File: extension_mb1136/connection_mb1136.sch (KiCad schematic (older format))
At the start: 6 parts, among them CN1 Conn_02x19_Odd_Even, CN2 Conn_02x19_Odd_Even, CN3 Conn_01x08, CN4 Conn_01x06, CN5 Conn_01x08, CN6 Conn_01x10

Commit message: update schema
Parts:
- added J1, J2: Conn_01x03, Connector_PinHeader_2.54mm:PinHeader_1x03_P2.54mm_Vertical, symbol Connector_Generic:Conn_01x03
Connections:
- net +5: no longer CN1.18 (Pin_18)
- net PC8: now also J1.2 (Pin_2)
- net PC9: now also J2.2 (Pin_2)
- new net +5V: CN1.18 (Pin_18)
- new net USB_DISCONNECT: J1.3 (Pin_3)
- new net USB_OWER_CURRENT: J2.1 (Pin_1)
- new net USB_POWER_SWITCH_ON: J1.1 (Pin_1)
- new net VBUS_DET: J2.3 (Pin_3)
- no-connect marks 0 -> 4
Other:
- moved on the sheet: CN1, CN2, CN3, CN4, CN5, CN6

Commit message: impruve schema
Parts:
- removed J1, J2: Conn_01x03, Connector_PinHeader_2.54mm:PinHeader_1x03_P2.54mm_Vertical, symbol Connector_Generic:Conn_01x03
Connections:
- net +5 is gone; now on net +5V: CN3.5 (Pin_5)
- net PC11: no longer CN1.4 (Pin_4)
- new net PD2: CN1.4 (Pin_4)
- no-connect marks 4 -> 8
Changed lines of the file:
@@
 PC11
 Text GLabel 2250 850  2    50   BiDi ~ 0
-PC11
+PD2
 Text GLabel 2250 950  2    50   UnSpc ~ 0
 E5V
@@
 +3V3
 Text GLabel 3500 1200 0    50   UnSpc ~ 0
-+5
++5V
 Text GLabel 3500 1300 0    50   UnSpc ~ 0
 GND
@@
 	950  1650 1350 1650
 Wire Wire Line
-	950  1750 1350 1750
-Wire Wire Line
 	950  1850 1350 1850
 Wire Wire Line
@@
 Wire Wire Line
 	1850 2550 2250 2550
-NoConn ~ 3800 800
+NoConn ~ 3900 800
 NoConn ~ 1350 1150
 NoConn ~ 1350 1250
@@
 Wire Wire Line
 	10250 1300 10650 1300
-Text GLabel 8450 3250 0    50   BiDi ~ 0
-PA11
-Text GLabel 8450 3450 0    50   BiDi ~ 0
-PA12
-Text GLabel 8450 3650 0    50   BiDi ~ 0
-PA10
-Text GLabel 9900 3250 2    50   BiDi ~ 0
-USB_DM
-Text GLabel 9900 3450 2    50   BiDi ~ 0
-USB_DP
-Text GLabel 9900 3650 2    50   BiDi ~ 0
-USB_ID
-Text GLabel 9900 3050 2    50   BiDi ~ 0
-USB_VBUS
-Text GLabel 8450 3050 0    50   BiDi ~ 0
-PA9
-Text GLabel 8450 4050 0    50   BiDi ~ 0
-PC8
-Text GLabel 8450 4750 0    50   BiDi ~ 0
-PC9
-$Comp
-L Connector_Generic:Conn_01x03 J1
-U 1 1 5FDC7556
-P 9000 4050
-F 0 "J1" H 9080 4092 50  0000 L CNN
-F 1 "Conn_01x03" H 9080 4001 50  0000 L CNN
-F 2 "Connector_PinHeader_2.54mm:PinHeader_1x03_P2.54mm_Vertical" H 9000 4050 50  0001 C CNN
-F 3 "~" H 9000 4050 50  0001 C CNN
-	1    9000 4050
-	1    0    0    -1
-$EndComp
-$Comp
-L Connector_Generic:Conn_01x03 J2
-U 1 1 5FDDBD38
-P 9000 4750
-F 0 "J2" H 9080 4792 50  0000 L CNN
-F 1 "Conn_01x03" H 9080 4701 50  0000 L CNN
-F 2 "Connector_PinHeader_2.54mm:PinHeader_1x03_P2.54mm_Vertical" H 9000 4750 50  0001 C CNN
-F 3 "~" H 9000 4750 50  0001 C CNN
-	1    9000 4750
-	1    0    0    -1
-$EndComp
-Text GLabel 9900 3850 2    50   BiDi ~ 0
-USB_POWER_SWITCH_ON
-Text GLabel 9900 4250 2    50   BiDi ~ 0
-USB_DISCONNECT
-Wire Wire Line
-	8800 3950 8650 3950
-Wire Wire Line
-	8650 3950 8650 3850
-Wire Wire Line
-	8650 3850 9900 3850
-Wire Wire Line
-	8800 4150 8650 4150
-Wire Wire Line
-	8650 4150 8650 4250
-Wire Wire Line
-	8650 4250 9900 4250
-Text GLabel 9900 4550 2    50   BiDi ~ 0
-USB_OWER_CURRENT
-Text GLabel 9900 4950 2    50   BiDi ~ 0
-VBUS_DET
-Wire Wire Line
-	8800 4650 8650 4650
-Wire Wire Line
-	8650 4650 8650 4550
-Wire Wire Line
-	8650 4550 9900 4550
-Wire Wire Line
-	8650 4950 9900 4950
-Wire Wire Line
-	8800 4850 8650 4850
-Wire Wire Line
-	8650 4850 8650 4950
-Wire Wire Line
-	8450 3250 9900 3250
-Wire Wire Line
-	8450 3450 9900 3450
-Wire Wire Line
-	8450 3650 9900 3650
-Wire Wire Line
-	8450 3050 9900 3050
-Wire Wire Line
-	8450 4050 8800 4050
-Wire Wire Line
-	8450 4750 8800 4750
-$Comp
-L power:+5V #PWR?
-U 1 1 6002CECB
-P 4150 3650
-F 0 "#PWR?" H 4150 3500 50  0001 C CNN
-F 1 "+5V" H 4165 3823 50  0000 C CNN
-F 2 "" H 4150 3650 50  0001 C CNN
-F 3 "" H 4150 3650 50  0001 C CNN
-	1    4150 3650
-	1    0    0    -1
-$EndComp
-Text GLabel 2950 3850 0    50   UnSpc ~ 0
-+5V
-Wire Wire Line
-	2950 3850 4150 3850
-Wire Wire Line
-	4150 3850 4150 3650
-$Comp
-L power:+3V3 #PWR?
-U 1 1 60036350
-P 4150 4300
-F 0 "#PWR?" H 4150 4150 50  0001 C CNN
-F 1 "+3V3" H 4165 4473 50  0000 C CNN
-F 2 "" H 4150 4300 50  0001 C CNN
-F 3 "" H 4150 4300 50  0001 C CNN
-	1    4150 4300
-	1    0    0    -1
-$EndComp
-Text GLabel 2950 4500 0    50   UnSpc ~ 0
-+3V3
-Wire Wire Line
-	2950 4500 4150 4500
-Wire Wire Line
-	4150 4500 4150 4300
-$Comp
-L power:GND #PWR?
-U 1 1 60042548
-P 4150 3050
-F 0 "#PWR?" H 4150 2800 50  0001 C CNN
-F 1 "GND" H 4155 2877 50  0000 C CNN
-F 2 "" H 4150 3050 50  0001 C CNN
-F 3 "" H 4150 3050 50  0001 C CNN
-	1    4150 3050
-	1    0    0    -1
-$EndComp
-Wire Wire Line
-	2950 2850 4150 2850
-Wire Wire Line
-	4150 2850 4150 3050
-Text GLabel 2950 2850 0    50   UnSpc ~ 0
-GND
 Text GLabel 2250 1650 2    50   UnSpc ~ 0
 GND
+Wire Wire Line
+	950  1750 1350 1750
+NoConn ~ 1850 1950
+NoConn ~ 10250 2400
+NoConn ~ 10250 2500
+NoConn ~ 10250 1100
 $EndSCHEMATC

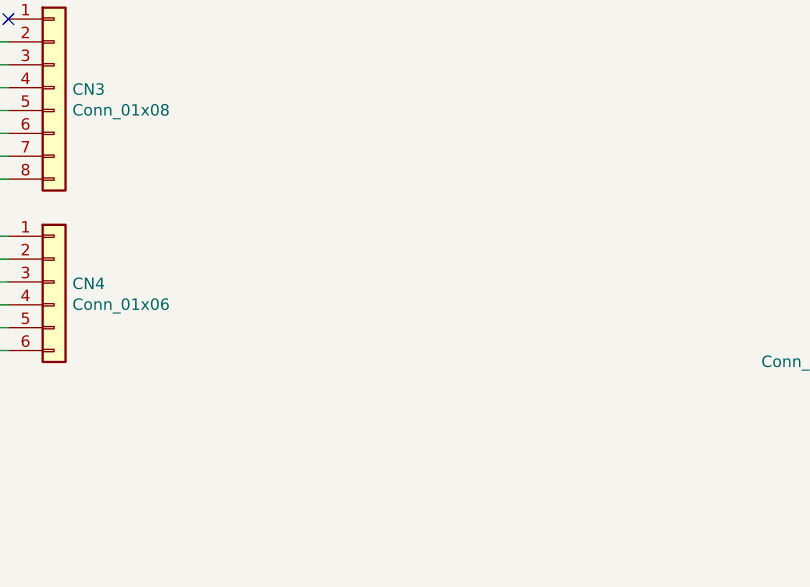
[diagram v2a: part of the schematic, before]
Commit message: add power flags
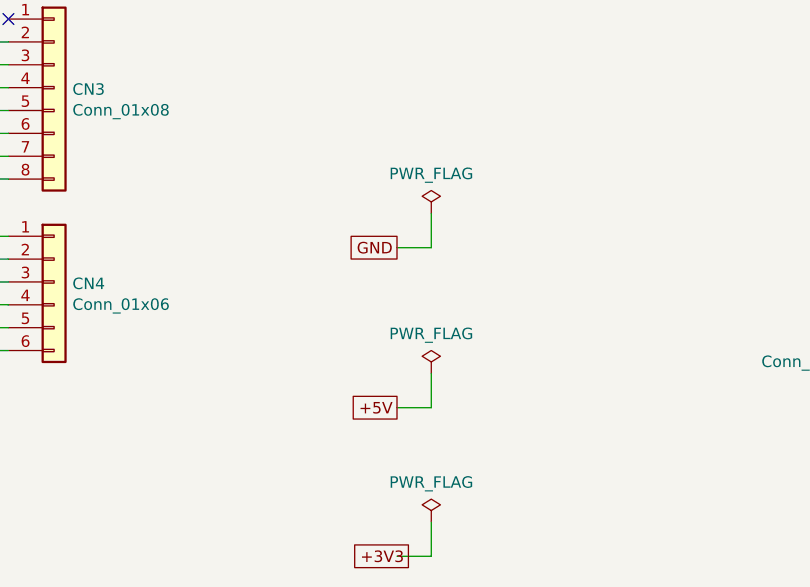
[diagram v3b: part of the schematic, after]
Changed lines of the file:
@@
 NoConn ~ 10250 2500
 NoConn ~ 10250 1100
+$Comp
+L power:PWR_FLAG #FLG0101
+U 1 1 5FE9552E
+P 5750 2350
+F 0 "#FLG0101" H 5750 2425 50  0001 C CNN
+F 1 "PWR_FLAG" H 5750 2523 50  0000 C CNN
+F 2 "" H 5750 2350 50  0001 C CNN
+F 3 "~" H 5750 2350 50  0001 C CNN
+	1    5750 2350
+	1    0    0    -1
+$EndComp
+Text GLabel 5600 2500 0    50   UnSpc ~ 0
++5V
+Wire Wire Line
+	5600 2500 5750 2500
+Wire Wire Line
+	5750 2500 5750 2350
+$Comp
+L power:PWR_FLAG #FLG0102
+U 1 1 5FE9D241
+P 5750 1650
+F 0 "#FLG0102" H 5750 1725 50  0001 C CNN
+F 1 "PWR_FLAG" H 5750 1823 50  0000 C CNN
+F 2 "" H 5750 1650 50  0001 C CNN
+F 3 "~" H 5750 1650 50  0001 C CNN
+	1    5750 1650
+	1    0    0    -1
+$EndComp
+Text GLabel 5600 1800 0    50   UnSpc ~ 0
+GND
+Wire Wire Line
+	5600 1800 5750 1800
+Wire Wire Line
+	5750 1800 5750 1650
+$Comp
+L power:PWR_FLAG #FLG0103
+U 1 1 5FEC77AE
+P 5750 3000
+F 0 "#FLG0103" H 5750 3075 50  0001 C CNN
+F 1 "PWR_FLAG" H 5750 3173 50  0000 C CNN
+F 2 "" H 5750 3000 50  0001 C CNN
+F 3 "~" H 5750 3000 50  0001 C CNN
+	1    5750 3000
+	1    0    0    -1
+$EndComp
+Text GLabel 5650 3150 0    50   UnSpc ~ 0
++3V3
+Wire Wire Line
+	5600 3150 5750 3150
+Wire Wire Line
+	5750 3150 5750 3000
 $EndSCHEMATC

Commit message: update pcb
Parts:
- added D3: D, Diode_SMD:D_0805_2012Metric_Pad1.15x1.40mm_HandSolder, symbol Device:D
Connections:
- net +5V: now also D3.2 (A)
- new net +5VD: D3.1 (K)
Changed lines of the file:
@@
 Wire Wire Line
 	5750 3150 5750 3000
+$Comp
+L Device:D D?
+U 1 1 6035D660
+P 5500 3900
+AR Path="/5FBD0FDB/6035D660" Ref="D?"  Part="1"
+AR Path="/5FBD0F73/6035D660" Ref="D3"  Part="1"
+F 0 "D3" H 5500 4117 50  0000 C CNN
+F 1 "D" H 5500 4026 50  0000 C CNN
+F 2 "Diode_SMD:D_0805_2012Metric_Pad1.15x1.40mm_HandSolder" H 5500 3900 50  0001 C CNN
+F 3 "~" H 5500 3900 50  0001 C CNN
+	1    5500 3900
+	-1   0    0    -1
+$EndComp
+$Comp
+L power:+5V #PWR?
+U 1 1 6035D666
+P 5200 3900
+F 0 "#PWR?" H 5200 3750 50  0001 C CNN
+F 1 "+5V" V 5215 4028 50  0000 L CNN
+F 2 "" H 5200 3900 50  0001 C CNN
+F 3 "" H 5200 3900 50  0001 C CNN
+	1    5200 3900
+	0    -1   -1   0
+$EndComp
+$Comp
+L power:+5VD #PWR?
+U 1 1 6035D66C
+P 5800 3900
+F 0 "#PWR?" H 5800 3750 50  0001 C CNN
+F 1 "+5VD" V 5815 4028 50  0000 L CNN
+F 2 "" H 5800 3900 50  0001 C CNN
+F 3 "" H 5800 3900 50  0001 C CNN
+	1    5800 3900
+	0    1    -1   0
+$EndComp
+Wire Wire Line
+	5200 3900 5350 3900
+$Comp
+L power:PWR_FLAG #FLG?
+U 1 1 6035D673
+P 5750 3750
+F 0 "#FLG?" H 5750 3825 50  0001 C CNN
+F 1 "PWR_FLAG" H 5750 3923 50  0000 C CNN
+F 2 "" H 5750 3750 50  0001 C CNN
+F 3 "~" H 5750 3750 50  0001 C CNN
+	1    5750 3750
+	1    0    0    -1
+$EndComp
+Wire Wire Line
+	5650 3900 5750 3900
+Wire Wire Line
+	5750 3750 5750 3900
+Connection ~ 5750 3900
+Wire Wire Line
+	5750 3900 5800 3900
 $EndSCHEMATC

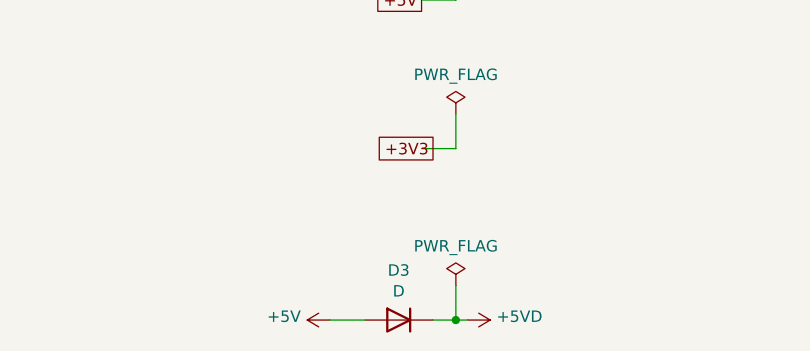
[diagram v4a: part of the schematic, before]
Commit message: change footprint for D2,D3
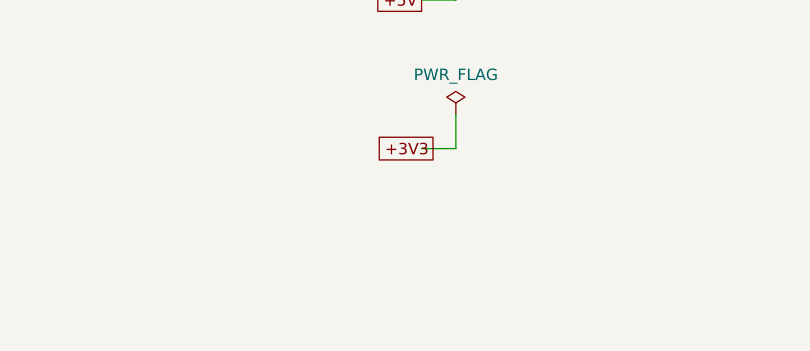
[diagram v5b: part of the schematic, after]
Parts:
- removed D3: D, Diode_SMD:D_0805_2012Metric_Pad1.15x1.40mm_HandSolder, symbol Device:D
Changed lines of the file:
@@
 Wire Wire Line
 	5750 3150 5750 3000
-$Comp
-L Device:D D?
-U 1 1 6035D660
-P 5500 3900
-AR Path="/5FBD0FDB/6035D660" Ref="D?"  Part="1"
-AR Path="/5FBD0F73/6035D660" Ref="D3"  Part="1"
-F 0 "D3" H 5500 4117 50  0000 C CNN
-F 1 "D" H 5500 4026 50  0000 C CNN
-F 2 "Diode_SMD:D_0805_2012Metric_Pad1.15x1.40mm_HandSolder" H 5500 3900 50  0001 C CNN
-F 3 "~" H 5500 3900 50  0001 C CNN
-	1    5500 3900
-	-1   0    0    -1
-$EndComp
-$Comp
-L power:+5V #PWR?
-U 1 1 6035D666
-P 5200 3900
-F 0 "#PWR?" H 5200 3750 50  0001 C CNN
-F 1 "+5V" V 5215 4028 50  0000 L CNN
-F 2 "" H 5200 3900 50  0001 C CNN
-F 3 "" H 5200 3900 50  0001 C CNN
-	1    5200 3900
-	0    -1   -1   0
-$EndComp
-$Comp
-L power:+5VD #PWR?
-U 1 1 6035D66C
-P 5800 3900
-F 0 "#PWR?" H 5800 3750 50  0001 C CNN
-F 1 "+5VD" V 5815 4028 50  0000 L CNN
-F 2 "" H 5800 3900 50  0001 C CNN
-F 3 "" H 5800 3900 50  0001 C CNN
-	1    5800 3900
-	0    1    -1   0
-$EndComp
-Wire Wire Line
-	5200 3900 5350 3900
-$Comp
-L power:PWR_FLAG #FLG?
-U 1 1 6035D673
-P 5750 3750
-F 0 "#FLG?" H 5750 3825 50  0001 C CNN
-F 1 "PWR_FLAG" H 5750 3923 50  0000 C CNN
-F 2 "" H 5750 3750 50  0001 C CNN
-F 3 "~" H 5750 3750 50  0001 C CNN
-	1    5750 3750
-	1    0    0    -1
-$EndComp
-Wire Wire Line
-	5650 3900 5750 3900
-Wire Wire Line
-	5750 3750 5750 3900
-Connection ~ 5750 3900
-Wire Wire Line
-	5750 3900 5800 3900
 $EndSCHEMATC
